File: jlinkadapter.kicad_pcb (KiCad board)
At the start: 2 copper layers, 43.5 x 34.5 mm, 7 parts, among them J1 Conn_02x05_Edge_connector, J2 Conn_02x05_Odd_Even, J3 Conn_01x05, J4 Conn_02x10_Odd_Even

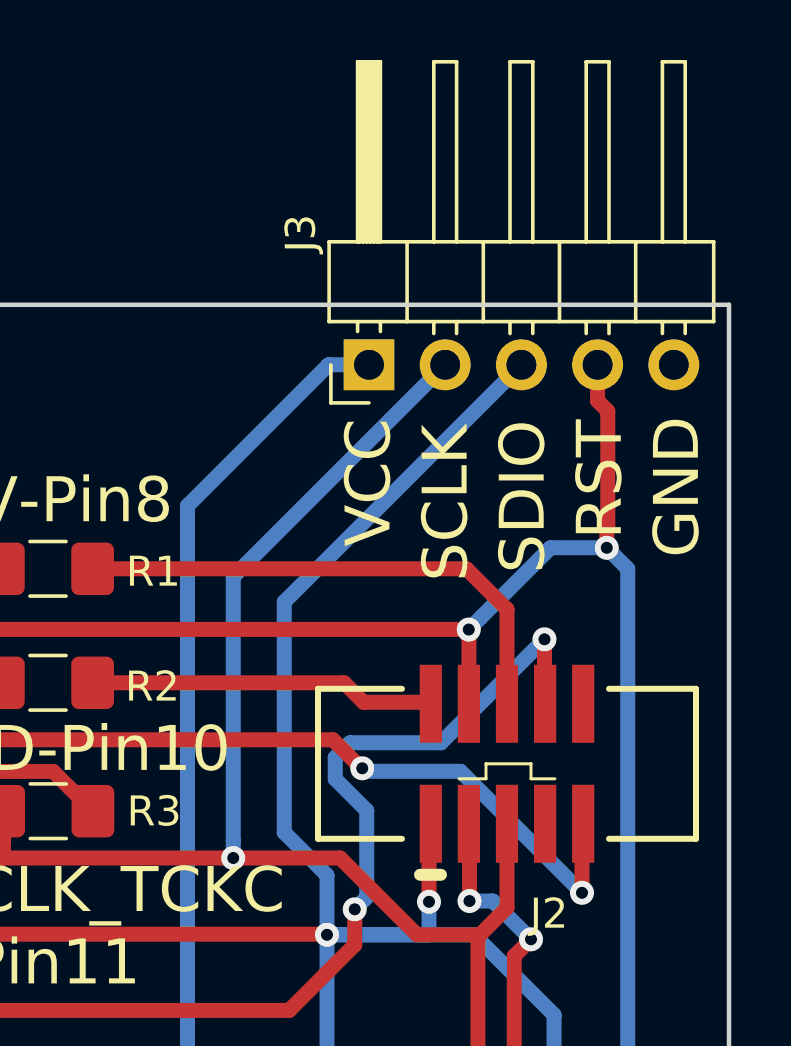
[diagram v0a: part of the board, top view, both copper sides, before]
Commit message: Small fixes, exporting gerbers for fab
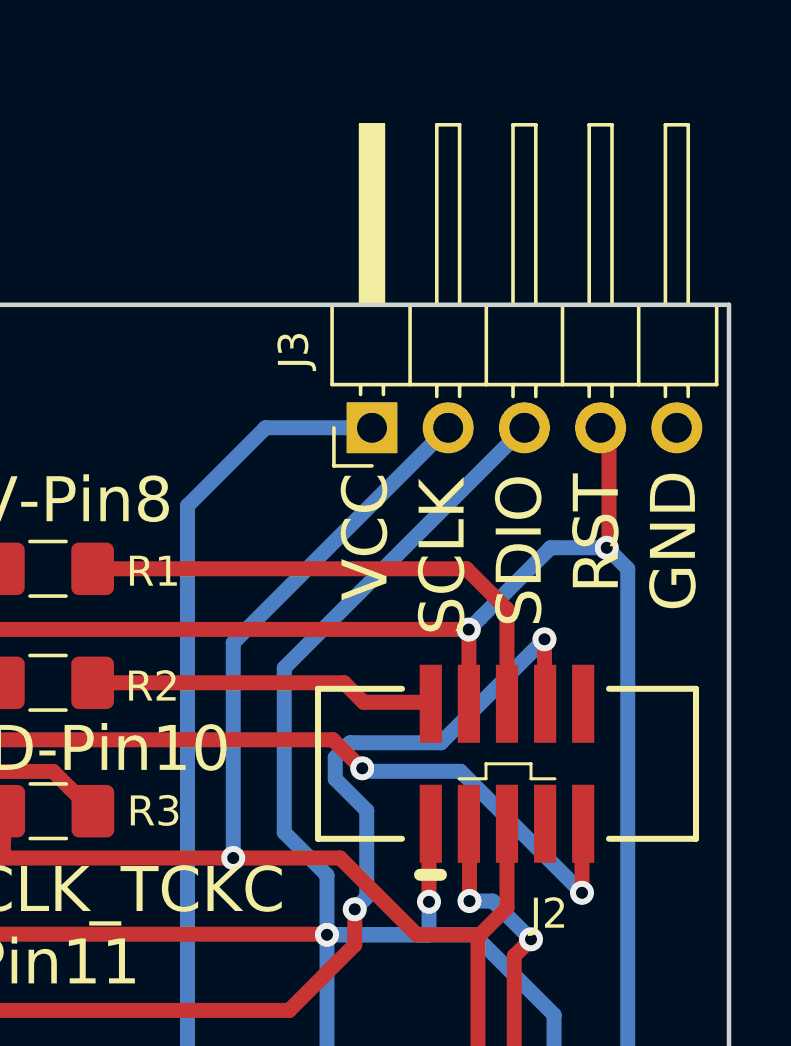
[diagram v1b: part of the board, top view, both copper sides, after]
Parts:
- moved J3 2.10 mm to (138.1, 57.6)
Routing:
- net /nRESET: track 72.9 -> 70.8 mm
- net /SWDIO_TMSC: track 77.9 -> 75.8 mm
- net /SWDCLK_TCKC: track 66.2 -> 64.1 mm
- net VCC: track 83.2 -> 82.4 mm
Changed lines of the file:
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@@
   (general
     (thickness 1.6)
-    (drawings 12)
-    (tracks 139)
+    (drawings 14)
+    (tracks 136)
     (zones 0)
     (modules 7)
@@
     (visible_elements FFFDFF7F)
     (pcbplotparams
-      (layerselection 0x010fc_ffffffff)
+      (layerselection 0x010f0_ffffffff)
       (usegerberextensions false)
       (usegerberattributes false)
@@
       (outputformat 1)
       (mirror false)
-      (drillshape 1)
+      (drillshape 0)
       (scaleselection 1)
-      (outputdirectory ""))
+      (outputdirectory "gerber"))
   )
   (net 0 "")
@@
   )
   (module Connector_PinHeader_2.54mm:PinHeader_1x05_P2.54mm_Horizontal (layer F.Cu)
-    (at 138 55.5 90)
+    (at 138.1 57.6 90)
     (descr "Through hole angled pin header, 1x05, 2.54mm pitch, 6mm pin length, single row")
     (tags "Through hole angled pin header THT 1x05 2.54mm single row")
-    (fp_text reference J3 (at 4.385 -2.27 90) (layer F.SilkS)
+    (fp_text reference J3 (at 2.6 -2.6 90) (layer F.SilkS)
       (effects (font (size 1 1) (thickness 0.15)))
     )
@@
     (pad "" np_thru_hole circle (at 4.8 -2.45) (size 1.7 1.7) (drill 1.7) (layers *.Cu *.Mask))
   )
+  (dimension 34.5 (width 0.3) (layer Dwgs.User)
+    (gr_text "34.500 mm" (at 157.5 70.75 270) (layer Dwgs.User)
+      (effects (font (size 1.5 1.5) (thickness 0.3)))
+    )
+    (feature1 (pts (xy 150 88) (xy 155.986421 88)))
+    (feature2 (pts (xy 150 53.5) (xy 155.986421 53.5)))
+    (crossbar (pts (xy 155.4 53.5) (xy 155.4 88)))
+    (arrow1a (pts (xy 155.4 88) (xy 154.813579 86.873496)))
+    (arrow1b (pts (xy 155.4 88) (xy 155.986421 86.873496)))
+    (arrow2a (pts (xy 155.4 53.5) (xy 154.813579 54.626504)))
+    (arrow2b (pts (xy 155.4 53.5) (xy 155.986421 54.626504)))
+  )
+  (dimension 43.5 (width 0.3) (layer Dwgs.User)
+    (gr_text "43.500 mm" (at 128.25 95.599999) (layer Dwgs.User)
+      (effects (font (size 1.5 1.5) (thickness 0.3)))
+    )
+    (feature1 (pts (xy 150 88) (xy 150 94.08642)))
+    (feature2 (pts (xy 106.5 88) (xy 106.5 94.08642)))
+    (crossbar (pts (xy 106.5 93.499999) (xy 150 93.499999)))
+    (arrow1a (pts (xy 150 93.499999) (xy 148.873496 94.08642)))
+    (arrow1b (pts (xy 150 93.499999) (xy 148.873496 92.913578)))
+    (arrow2a (pts (xy 106.5 93.499999) (xy 107.626504 94.08642)))
+    (arrow2b (pts (xy 106.5 93.499999) (xy 107.626504 92.913578)))
+  )
   (gr_text GND-Pin10 (at 127.79 68.31) (layer F.SilkS)
     (effects (font (size 1.5 1.5) (thickness 0.3)))
@@
     (effects (font (size 1.5 1.5) (thickness 0.3)))
   )
-  (gr_text GND (at 148.27 59.57 90) (layer F.SilkS)
-    (effects (font (size 1.5 1.5) (thickness 0.3)))
-  )
-  (gr_text RST (at 145.7 59.32 90) (layer F.SilkS)
-    (effects (font (size 1.5 1.5) (thickness 0.3)))
-  )
-  (gr_text SDIO (at 143.13 59.891428 90) (layer F.SilkS)
-    (effects (font (size 1.5 1.5) (thickness 0.3)))
-  )
-  (gr_text SCLK (at 140.56 60.105714 90) (layer F.SilkS)
-    (effects (font (size 1.5 1.5) (thickness 0.3)))
-  )
-  (gr_text VCC (at 137.99 59.427142 90) (layer F.SilkS)
+  (gr_text GND (at 148.17 61.37 90) (layer F.SilkS)
+    (effects (font (size 1.5 1.5) (thickness 0.3)))
+  )
+  (gr_text RST (at 145.6 61.12 90) (layer F.SilkS)
+    (effects (font (size 1.5 1.5) (thickness 0.3)))
+  )
+  (gr_text SDIO (at 143.03 61.691428 90) (layer F.SilkS)
+    (effects (font (size 1.5 1.5) (thickness 0.3)))
+  )
+  (gr_text SCLK (at 140.46 61.905714 90) (layer F.SilkS)
+    (effects (font (size 1.5 1.5) (thickness 0.3)))
+  )
+  (gr_text VCC (at 137.89 61.227142 90) (layer F.SilkS)
     (effects (font (size 1.5 1.5) (thickness 0.3)))
   )
@@
   (segment (start 137.74237 83.09237) (end 138.94237 83.09237) (width 0.5) (layer B.Cu) (net 2))
   (segment (start 138.94237 83.09237) (end 140.02 84.17) (width 0.5) (layer B.Cu) (net 2))
-  (segment (start 135.175 63.405) (end 143.08 55.5) (width 0.5) (layer B.Cu) (net 2))
-  (segment (start 135.175 71.09) (end 135.175 63.405) (width 0.5) (layer B.Cu) (net 2))
+  (segment (start 135.175 65.605) (end 143.18 57.6) (width 0.5) (layer B.Cu) (net 2))
+  (segment (start 135.175 71.09) (end 135.175 65.605) (width 0.5) (layer B.Cu) (net 2))
   (segment (start 136.6 72.515) (end 135.175 71.09) (width 0.5) (layer B.Cu) (net 2))
   (segment (start 136.6 74.5) (end 136.6 72.515) (width 0.5) (layer B.Cu) (net 2))
@@
   (segment (start 133.475 71.94) (end 137.04 71.94) (width 0.5) (layer F.Cu) (net 3))
   (via (at 133.475006 71.94) (size 0.8) (drill 0.4) (layers F.Cu B.Cu) (net 3))
-  (segment (start 133.475006 62.564994) (end 133.475006 71.374315) (width 0.5) (layer B.Cu) (net 3))
-  (segment (start 140.54 55.5) (end 133.475006 62.564994) (width 0.5) (layer B.Cu) (net 3))
-  (segment (start 133.475006 71.374315) (end 133.475006 71.94) (width 0.5) (layer B.Cu) (net 3))
   (segment (start 133.475 71.94) (end 133.475006 71.94) (width 0.5) (layer F.Cu) (net 3))
   (segment (start 125.8125 71.9275) (end 125.8 71.94) (width 0.5) (layer F.Cu) (net 3))
@@
   (segment (start 125.8225 71.355) (end 125.8125 71.365) (width 0.5) (layer F.Cu) (net 3))
   (segment (start 125.8225 70.38) (end 125.8225 71.355) (width 0.5) (layer F.Cu) (net 3))
+  (segment (start 133.475006 64.764994) (end 140.64 57.6) (width 0.5) (layer B.Cu) (net 3))
+  (segment (start 133.475006 71.94) (end 133.475006 64.764994) (width 0.5) (layer B.Cu) (net 3))
   (segment (start 145.44 82.70763) (end 145.44 81.63) (width 0.5) (layer B.Cu) (net 4))
   (segment (start 145.44 84.693762) (end 145.44 82.70763) (width 0.5) (layer B.Cu) (net 4))
@@
   (segment (start 141.687999 85.382001) (end 144.751761 85.382001) (width 0.5) (layer B.Cu) (net 4))
   (segment (start 140.36 86.71) (end 141.687999 85.382001) (width 0.5) (layer B.Cu) (net 4))
-  (segment (start 145.62 56.702081) (end 145.62 55.5) (width 0.5) (layer F.Cu) (net 4))
-  (segment (start 145.960001 57.042082) (end 145.62 56.702081) (width 0.5) (layer F.Cu) (net 4))
   (via (at 145.925 61.6) (size 0.8) (drill 0.4) (layers F.Cu B.Cu) (net 4))
   (segment (start 145.44 80.55237) (end 146.625 79.36737) (width 0.5) (layer B.Cu) (net 4))
@@
   (segment (start 146.625 62.3) (end 145.925 61.6) (width 0.5) (layer B.Cu) (net 4))
   (segment (start 146.625 79.36737) (end 146.625 62.3) (width 0.5) (layer B.Cu) (net 4))
-  (segment (start 145.960001 60.999314) (end 145.960001 57.042082) (width 0.5) (layer F.Cu) (net 4))
-  (segment (start 145.925 61.034315) (end 145.960001 60.999314) (width 0.5) (layer F.Cu) (net 4))
-  (segment (start 145.925 61.6) (end 145.925 61.034315) (width 0.5) (layer F.Cu) (net 4))
   (segment (start 141.724999 63.925001) (end 141.325 64.325) (width 0.5) (layer B.Cu) (net 4))
   (segment (start 141.33 66.8) (end 141.33 64.32) (width 0.5) (layer F.Cu) (net 4))
@@
   (segment (start 144.05 61.6) (end 141.724999 63.925001) (width 0.5) (layer B.Cu) (net 4))
   (segment (start 112.7 64.32) (end 141.33 64.32) (width 0.5) (layer F.Cu) (net 4))
+  (segment (start 146 61.525) (end 145.925 61.6) (width 0.5) (layer F.Cu) (net 4))
+  (segment (start 146 57.88) (end 146 61.525) (width 0.5) (layer F.Cu) (net 4))
+  (segment (start 145.72 57.6) (end 146 57.88) (width 0.5) (layer F.Cu) (net 4))
   (via (at 123.47 66.11) (size 0.8) (drill 0.4) (layers F.Cu B.Cu) (net 5))
   (segment (start 125.8025 66.11) (end 125.8125 66.1) (width 0.5) (layer F.Cu) (net 5))
@@
   (segment (start 114.6636 82.7) (end 131.95 82.7) (width 0.5) (layer F.Cu) (net 6))
   (segment (start 131.95 82.7) (end 139.29 82.7) (width 0.5) (layer F.Cu) (net 6))
-  (segment (start 136.65 55.5) (end 138 55.5) (width 0.5) (layer B.Cu) (net 6))
-  (segment (start 131.95 60.2) (end 136.65 55.5) (width 0.5) (layer B.Cu) (net 6))
   (segment (start 131.95 82.7) (end 131.95 60.2) (width 0.5) (layer B.Cu) (net 6))
+  (segment (start 134.55 57.6) (end 138.1 57.6) (width 0.5) (layer B.Cu) (net 6))
+  (segment (start 131.95 60.2) (end 134.55 57.6) (width 0.5) (layer B.Cu) (net 6))
   (via (at 137.525 73.65) (size 0.8) (drill 0.4) (layers F.Cu B.Cu) (net 7))
   (segment (start 135.338002 77.02) (end 137.525 74.833002) (width 0.5) (layer F.Cu) (net 7))
